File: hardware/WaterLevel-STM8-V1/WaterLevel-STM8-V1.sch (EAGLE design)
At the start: 22 parts, among them IC2 STM8S003F3P6, K1 RELAY-SPDT

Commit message: #1 New PCB update
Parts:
- removed D5, D6: (no value), electroShri:LED-5MM-REC5MM
- removed J1, J2: (no value), electroShri:SCREW-CONN_03-SCREW-5MM
- added A0, SCL, SDA: TPSQTP20R, testpad:TPSQTP20R
- added AC_IN, MOTOR, TANK: (no value), electroShri:SCREW-CONN_03-SCREW-5MM
- added C1, C2: 1uF, eventHorizon:CAP_CERAMIC0805
- added FULL, LOW, SYS: (no value), electroShri:LED-5MM-REC5MM
- added GOLD_ORB_SM1: OSHWLOGOLOGO16MM, electroShri:OSHWLOGOLOGO16MM
- added J4: (no value), SparkFun-Connectors:CONN_04PTH
- added J5: (no value), electroShri:6_PIN_SERIAL_TARGETSILK
- added R10, R9: 10K, eventHorizon:RESISTOR0805
- added R6, R7, R8: 330, eventHorizon:RESISTOR0805
- added VR1: LM1117MPX-3.3, electroShri:LM1117MPX-3.3
- D2, D4: value (none) -> TPSQTP20R; device electroShri:LED-5MM-REC5MM -> testpad:TPSQTP20R
- J3: device electroShri:SCREW-CONN_03-SCREW-5MM -> electroShri:2PIN-2.54MM-POLARPOLAR
- R1, R5: device eventHorizon:RESISTOR0603 -> eventHorizon:RESISTOR0805
- R2, R3: value (none) -> 10K
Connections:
- removed net D0(RX): R5.2
- new net EARTH: AC_IN.3, MOTOR.3
- new net LIVE: AC_IN.1, K1.MAIN, PS1.AC1
- new net LIVE-MTR: K1.NC, MOTOR.1
- new net N$6: FULL.A, R7.1
- new net N$7: LOW.A, R8.1
- new net NUTRAL: AC_IN.2, MOTOR.2, PS1.AC2
- net +5V: now also C1.P$1, D1.K, J3.1, K1.COIL1, PS1.+VO, VR1.VIN
- net D13: now also R6.2
- net GND: now also C1.P$2, C2.P$2, FULL.C, J3.2, J4.2, J5.GND, LOW.C, PS1.-VO, SYS.C, TANK.3, VR1.GND
- net N$1: now also R6.1, SYS.A; no longer D1.K, K1.COIL1
- net PA1/D0: now also D4.TP
- net PA3/SS/D2~: now also D2.TP
- net PC3/D5~: now also R5.2
- net PC4/D6~/A0: now also A0.TP
- net PC6/D8~: now also R9.2, TANK.2
- net PC7/D9~: now also R10.2, TANK.1
- net PD2/D11/A1: now also R8.2
- net PD3/D12~/A2: now also R7.2
- net RST: now also J4.1
- net RX: now also J5.TXO
- net SCL: now also SCL.TP
- net SDA: now also SDA.TP
- net SWIM/D10: now also J4.3
- net TX: now also J5.RXI
- net VDD: now also C2.P$1, J4.4, J5.VCC, R10.1, R9.1, VR1.VOUT_2, VR1.VOUT_4
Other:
- moved on the sheet: D3, PS1, Q2, R1, R5, SG1

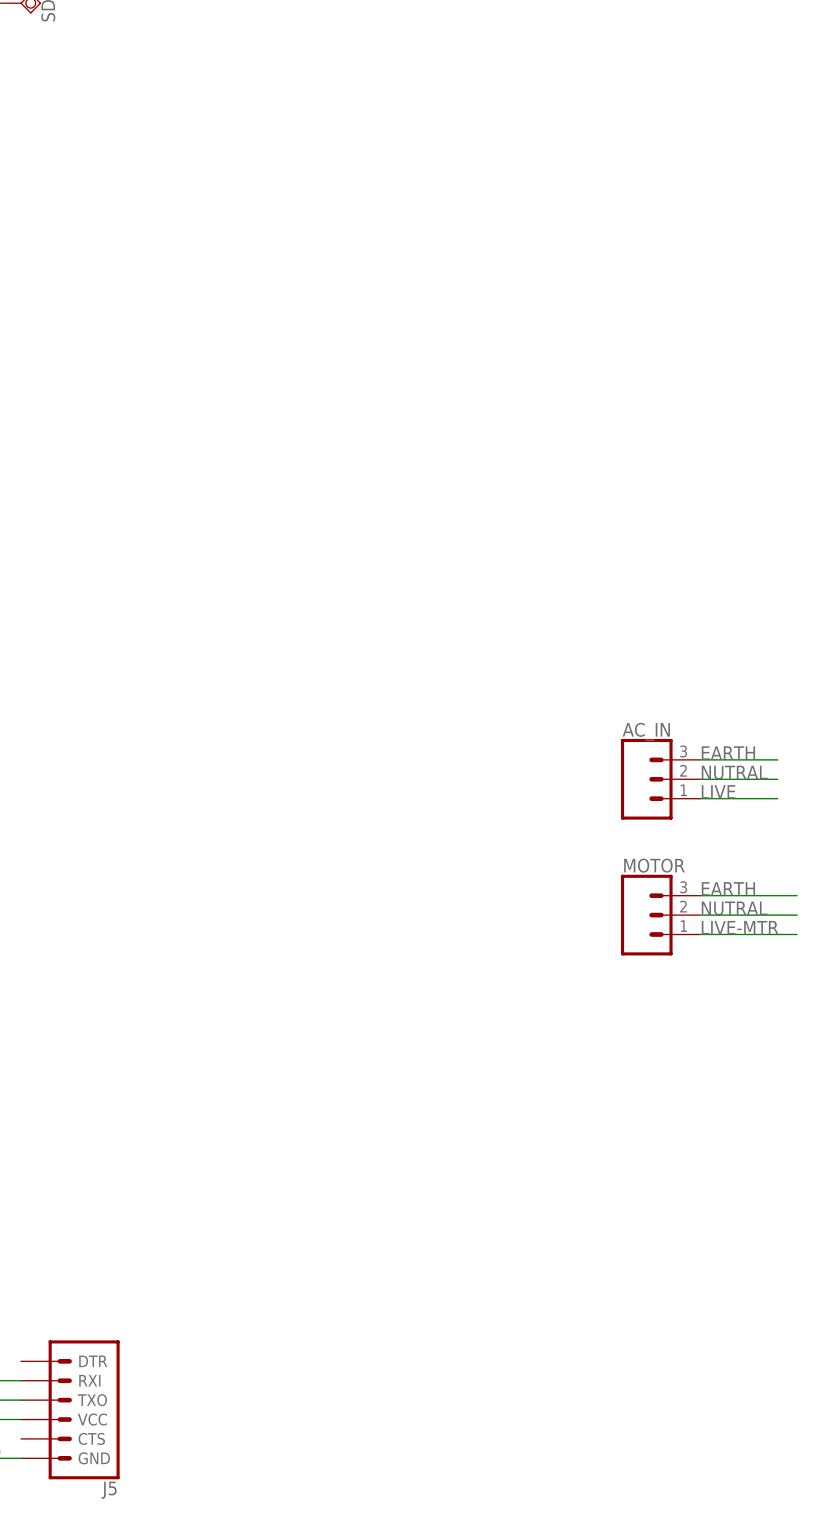
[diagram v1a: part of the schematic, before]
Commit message: Added I2C connector and  Manual Switch to the board
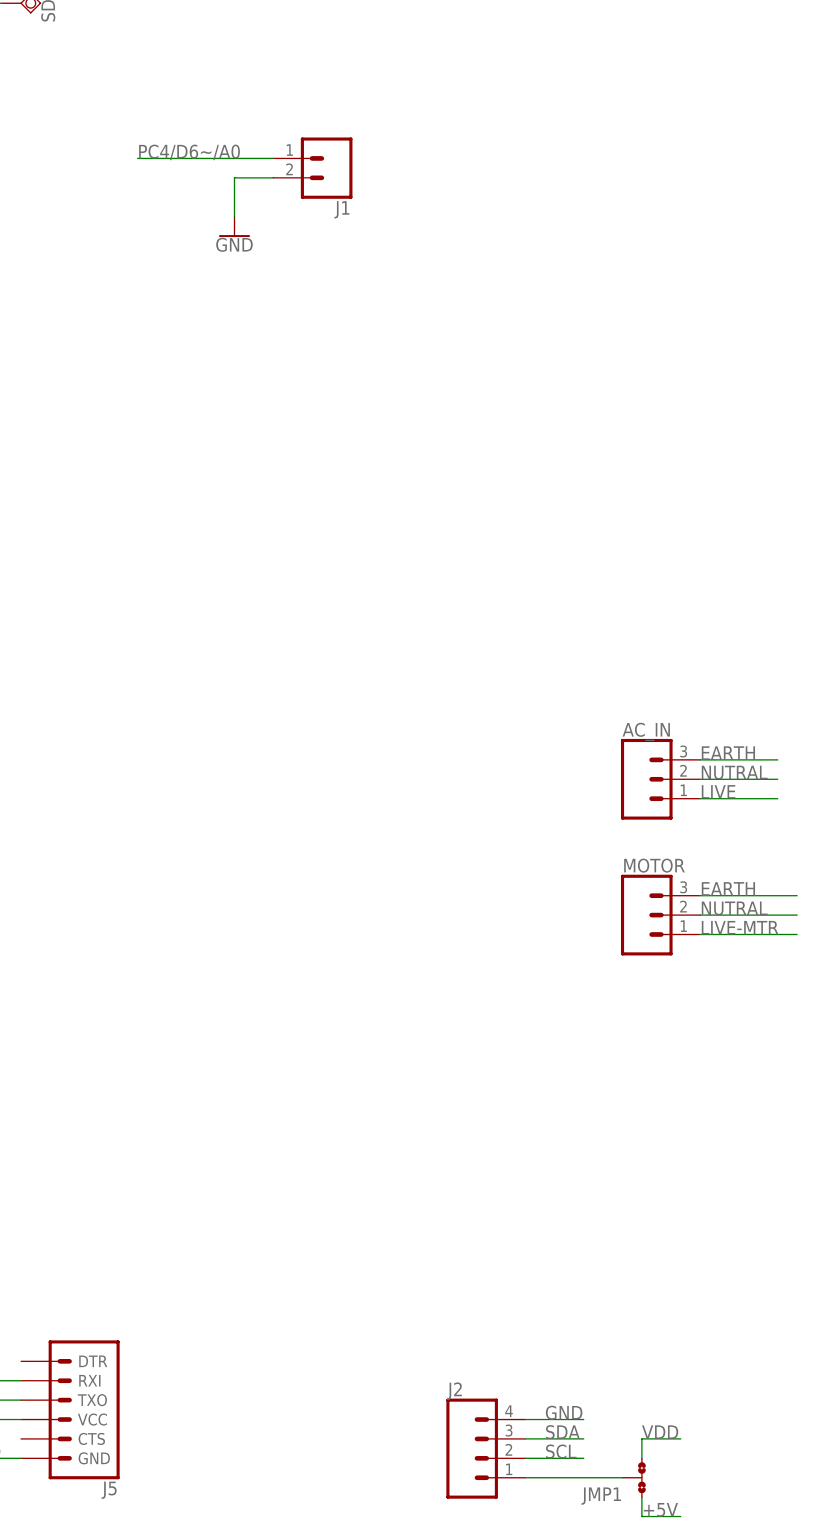
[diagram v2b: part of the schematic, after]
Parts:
- added J1: (no value), electroShri:2PIN-2.54MM-POLARPOLAR
- added J2: (no value), SparkFun-Connectors:CONN_04PTH
- added JMP1: (no value), PatternAgents-ProtoPads:JMP-3-NO
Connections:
- new net N$8: J2.1, JMP1.2
- net +5V: now also JMP1.1
- net GND: now also J1.2, J2.4
- net PC4/D6~/A0: now also J1.1
- net SCL: now also J2.2
- net SDA: now also J2.3
- net VDD: now also JMP1.3
